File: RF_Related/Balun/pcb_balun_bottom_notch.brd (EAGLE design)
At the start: 39 x 30 mm, 4 parts, among them T1 ADT1-1WT+, X1 SMA-142-0701-801/806, X2 SMA-142-0701-801/806, X3 SMA-142-0701-801/806

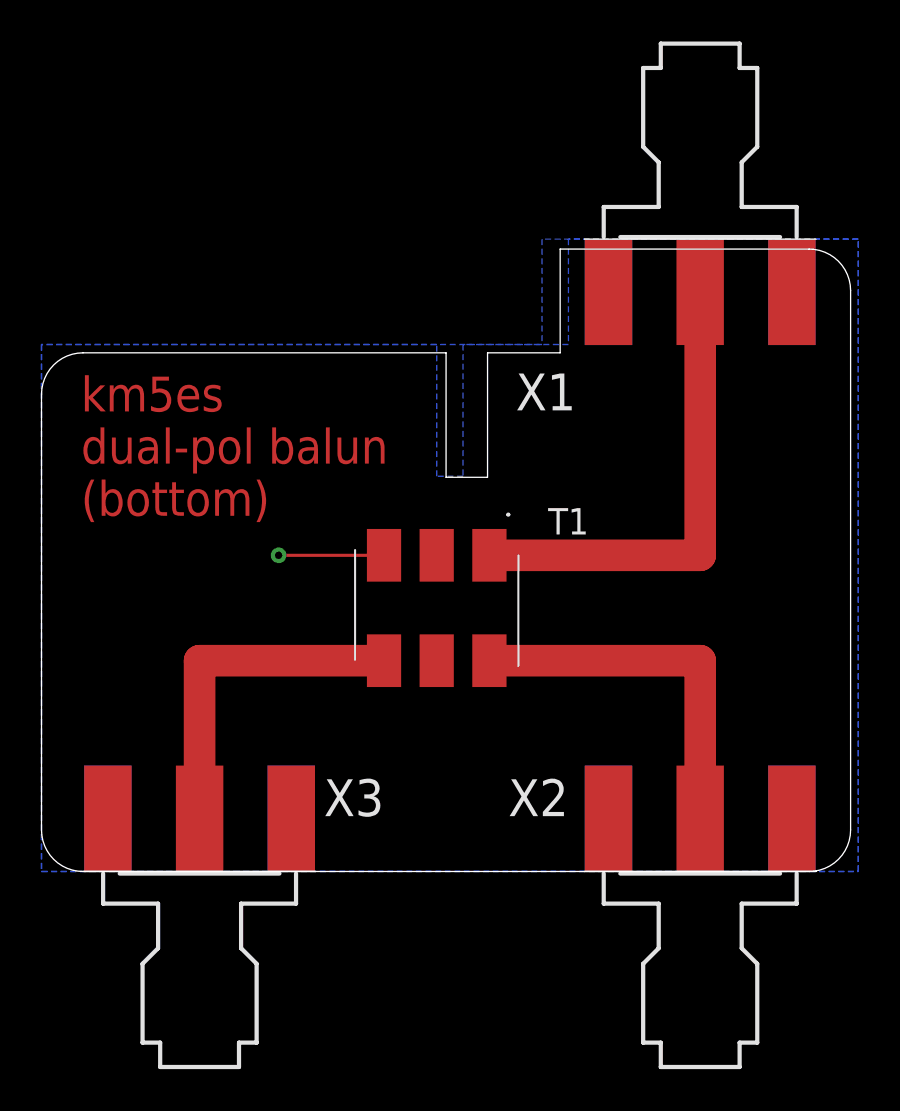
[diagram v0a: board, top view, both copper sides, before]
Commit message: balun is ready. do final checks on other boards before sending them in. 3D model of drone now has GPSDO antenna and more in the payload.
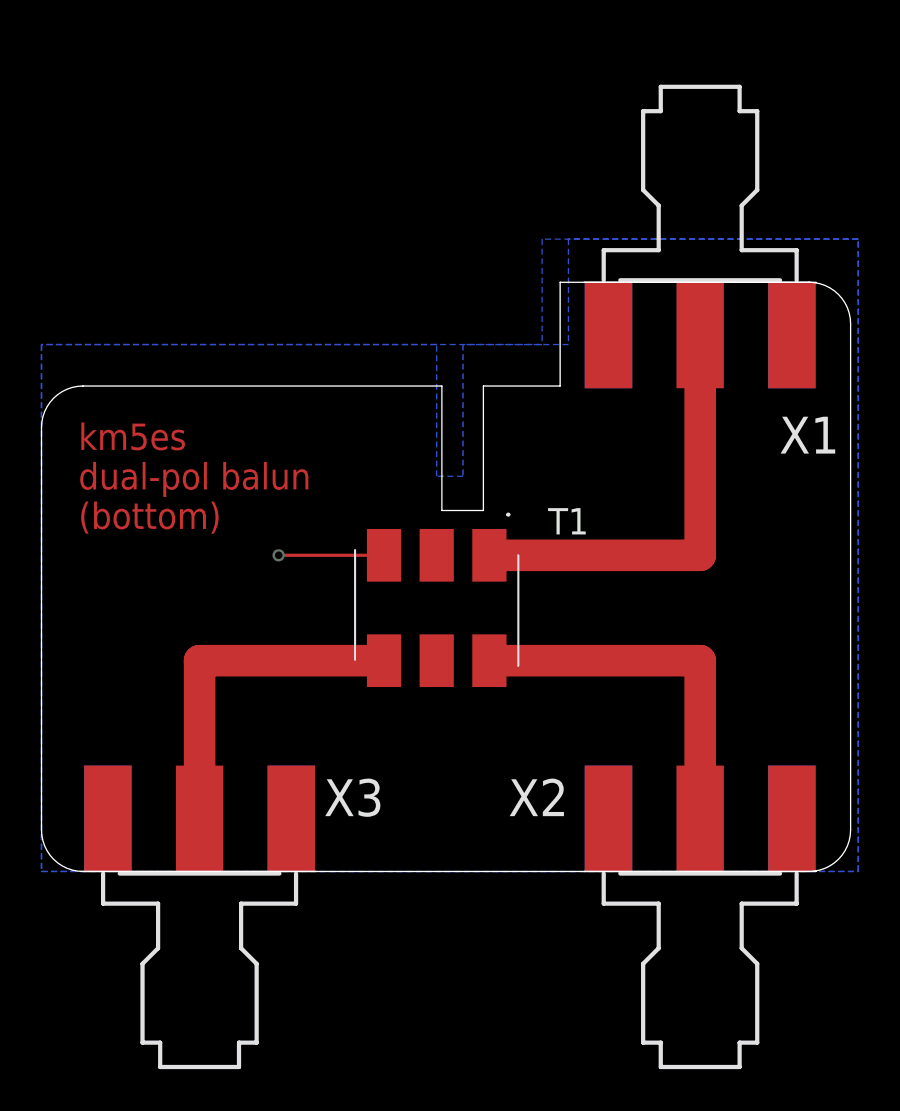
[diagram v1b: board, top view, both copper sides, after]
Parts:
- moved X1 2.08 mm to (31.8, 28.4)
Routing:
- net N$1: track 22.8 -> 20.8 mm
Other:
- board size 39 x 30 mm -> 39 x 28.4 mm
